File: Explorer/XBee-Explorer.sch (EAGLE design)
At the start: 31 parts, among them U2 XBEE-1B3, U3 MIC5205 3.3V, U4 FT231XS, X1 USBSMD

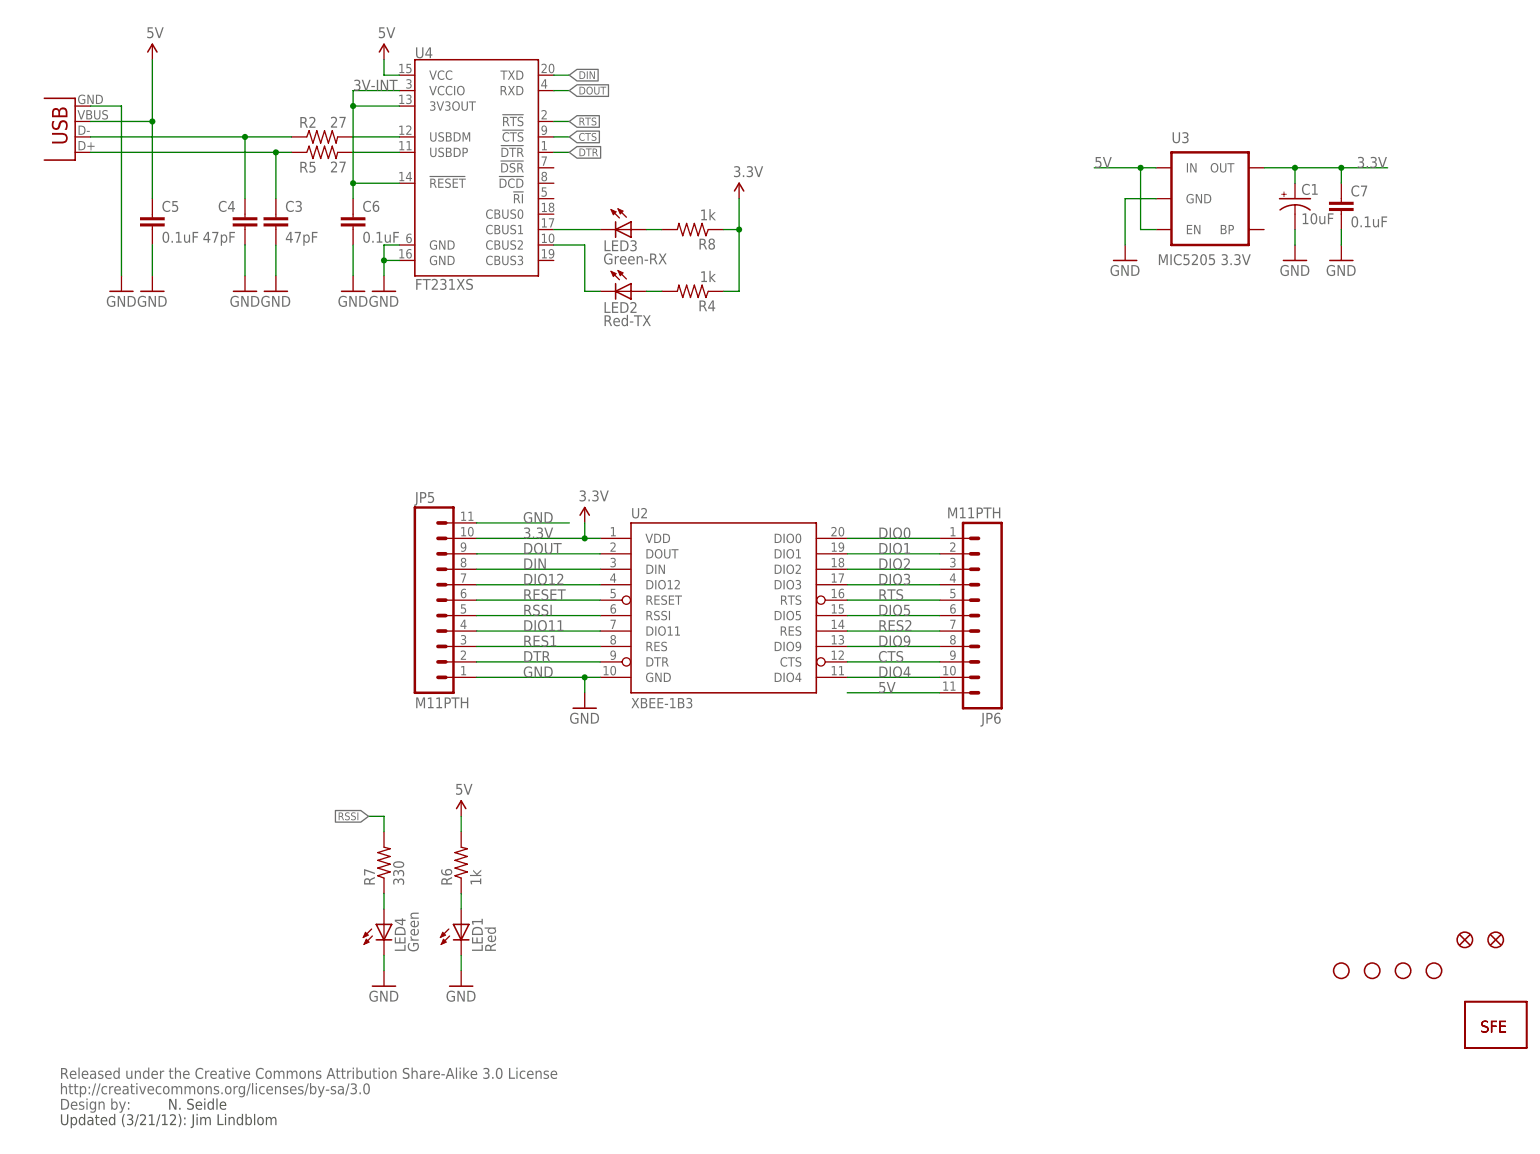
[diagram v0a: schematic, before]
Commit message: Added jumper to disconnect RSSI LED, moved silk
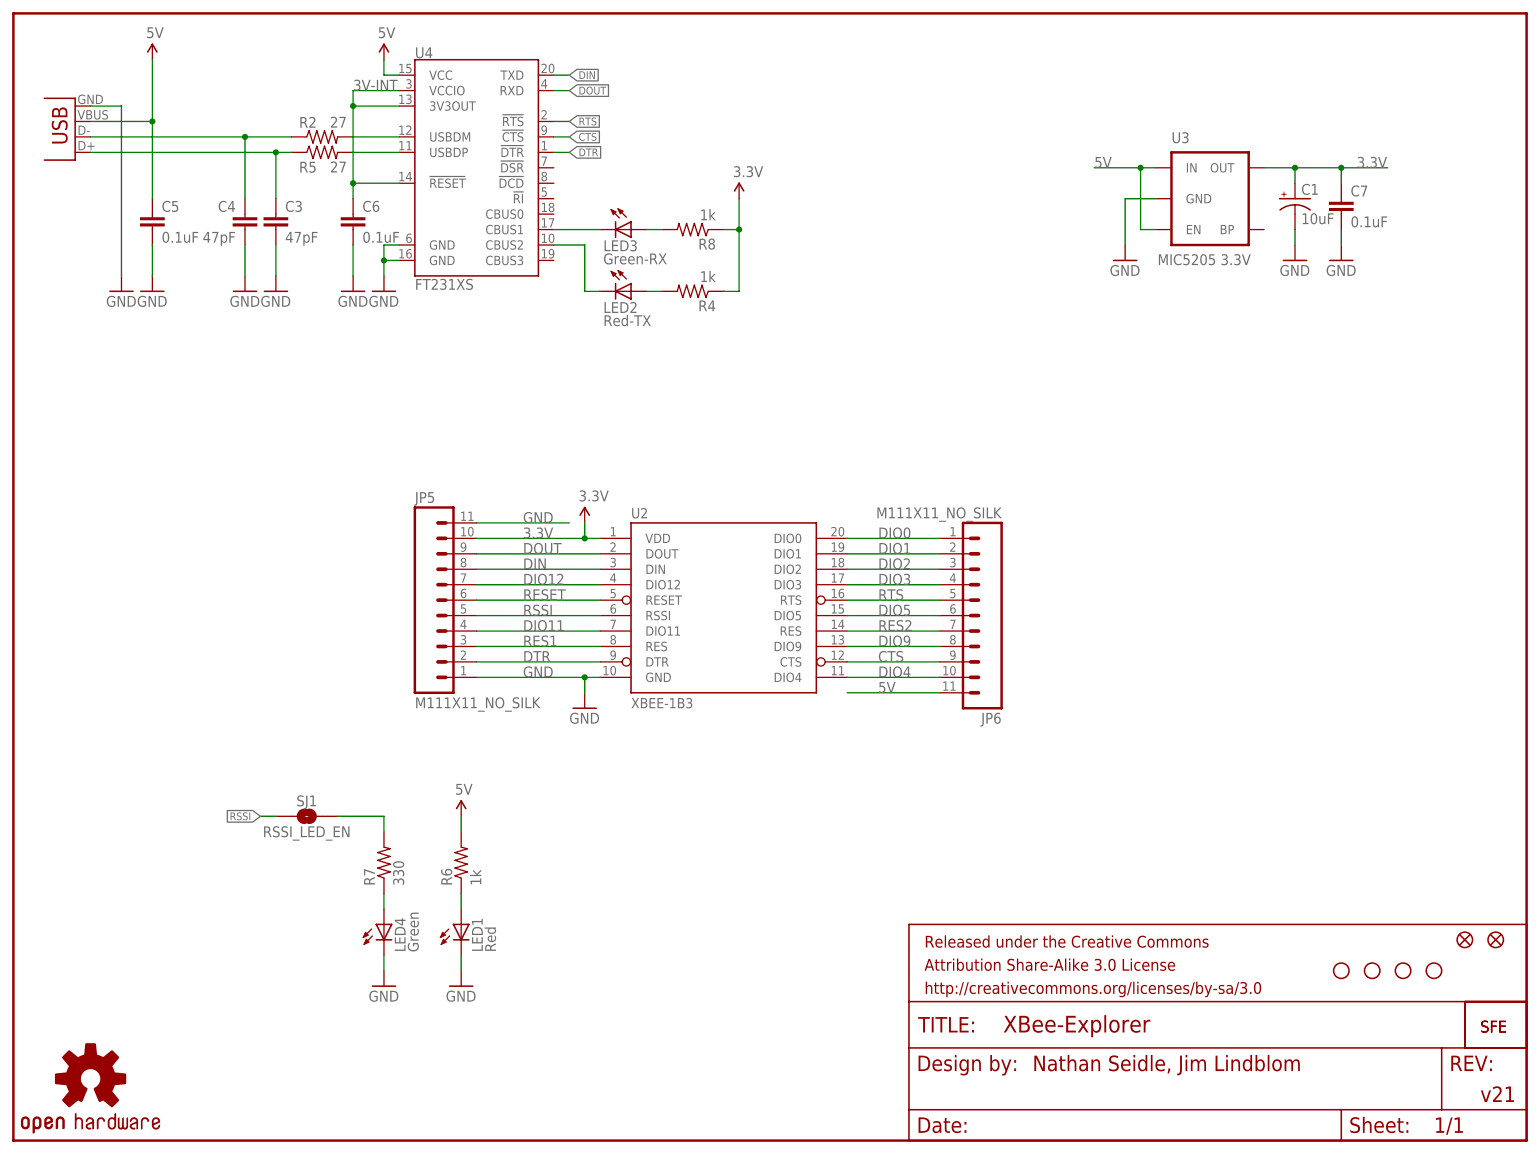
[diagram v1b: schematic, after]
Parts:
- removed U$2: CREATIVE_COMMONS, SparkFun:CREATIVE_COMMONS
- added FRAME1: FRAME-LETTER, SparkFun-Aesthetics:FRAME-LETTER
- added LOGO1: OSHW-LOGOS, SparkFun-Aesthetics:OSHW-LOGOS
- added SJ1: RSSI_LED_EN, SparkFun-Passives:SOLDERJUMPERTRACE
- JP5, JP6: value M11PTH -> M111X11_NO_SILK; device SparkFun-Connectors:M11PTH -> SparkFun-Connectors:M111X11_NO_SILK
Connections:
- new net N$9: R7.2, SJ1.2
- net RSSI: now also SJ1.1; no longer R7.2
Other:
- note added: "Nathan Seidle, Jim Lindblom"
- note added: "v21"
- note removed: "N. Seidle"
- note removed: "Updated (3/21/12): Jim Lindblom"

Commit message: Adding reset button, jumpers on UART ctrl lines
Reset button required moving LEDs around.
Adding jumpers on DTR, CTS, and RTS because they're not present on some
XBee compatible boards. Those pins can be used as GPIOs.
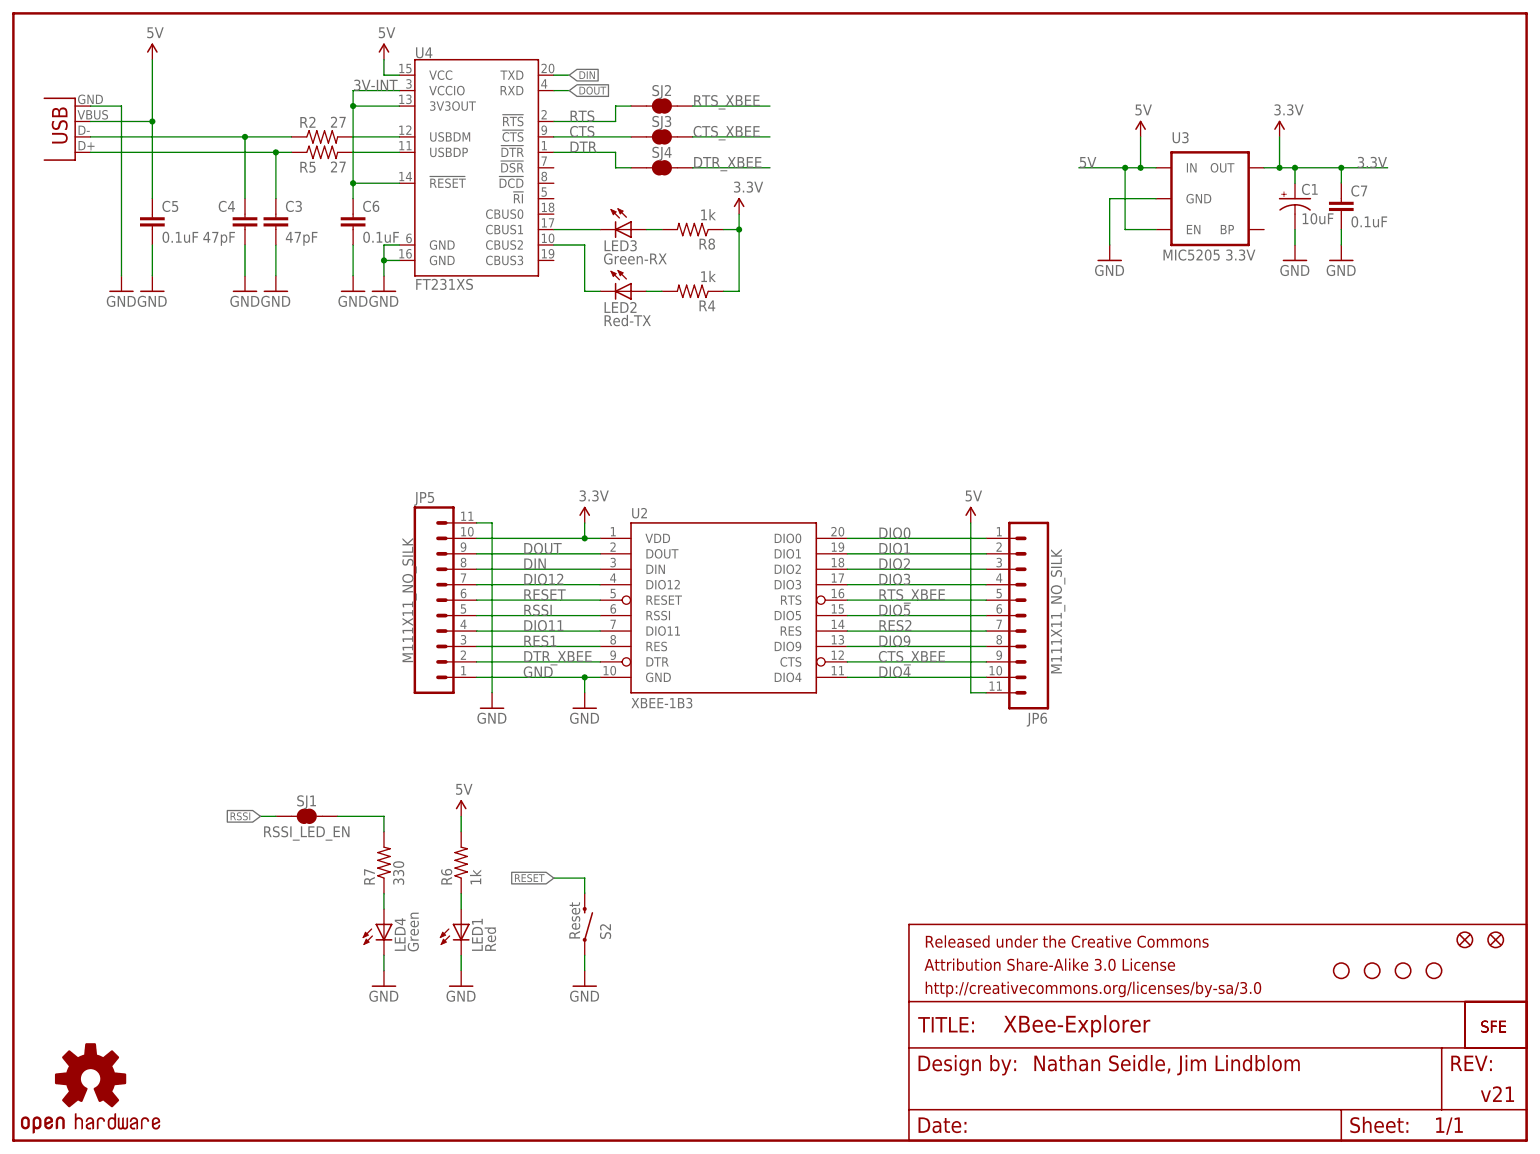
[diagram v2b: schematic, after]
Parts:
- added S2: Reset, SparkFun-Electromechanical:SWITCH-MOMENTARY-2SMD
- added SJ2: CTS_EN, SparkFun-Passives:SOLDERJUMPERTRACE
- added SJ3: RTS_EN, SparkFun-Passives:SOLDERJUMPERTRACE
- added SJ4: DTR, SparkFun-Passives:SOLDERJUMPERTRACE
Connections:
- new net CTS_XBEE: JP6.9, SJ3.2, U2.CTS
- new net DTR_XBEE: JP5.2, SJ4.2, U2.DTR
- new net RTS_XBEE: JP6.5, SJ2.2, U2.RTS
- net CTS: now also SJ3.1; no longer JP6.9, U2.CTS
- net DTR: now also SJ4.1; no longer JP5.2, U2.DTR
- net GND: now also S2.1
- net RESET: now also S2.2
- net RTS: now also SJ2.1; no longer JP6.5, U2.RTS
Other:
- moved on the sheet: JP6

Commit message: Increasing fiducial size and LED footprint
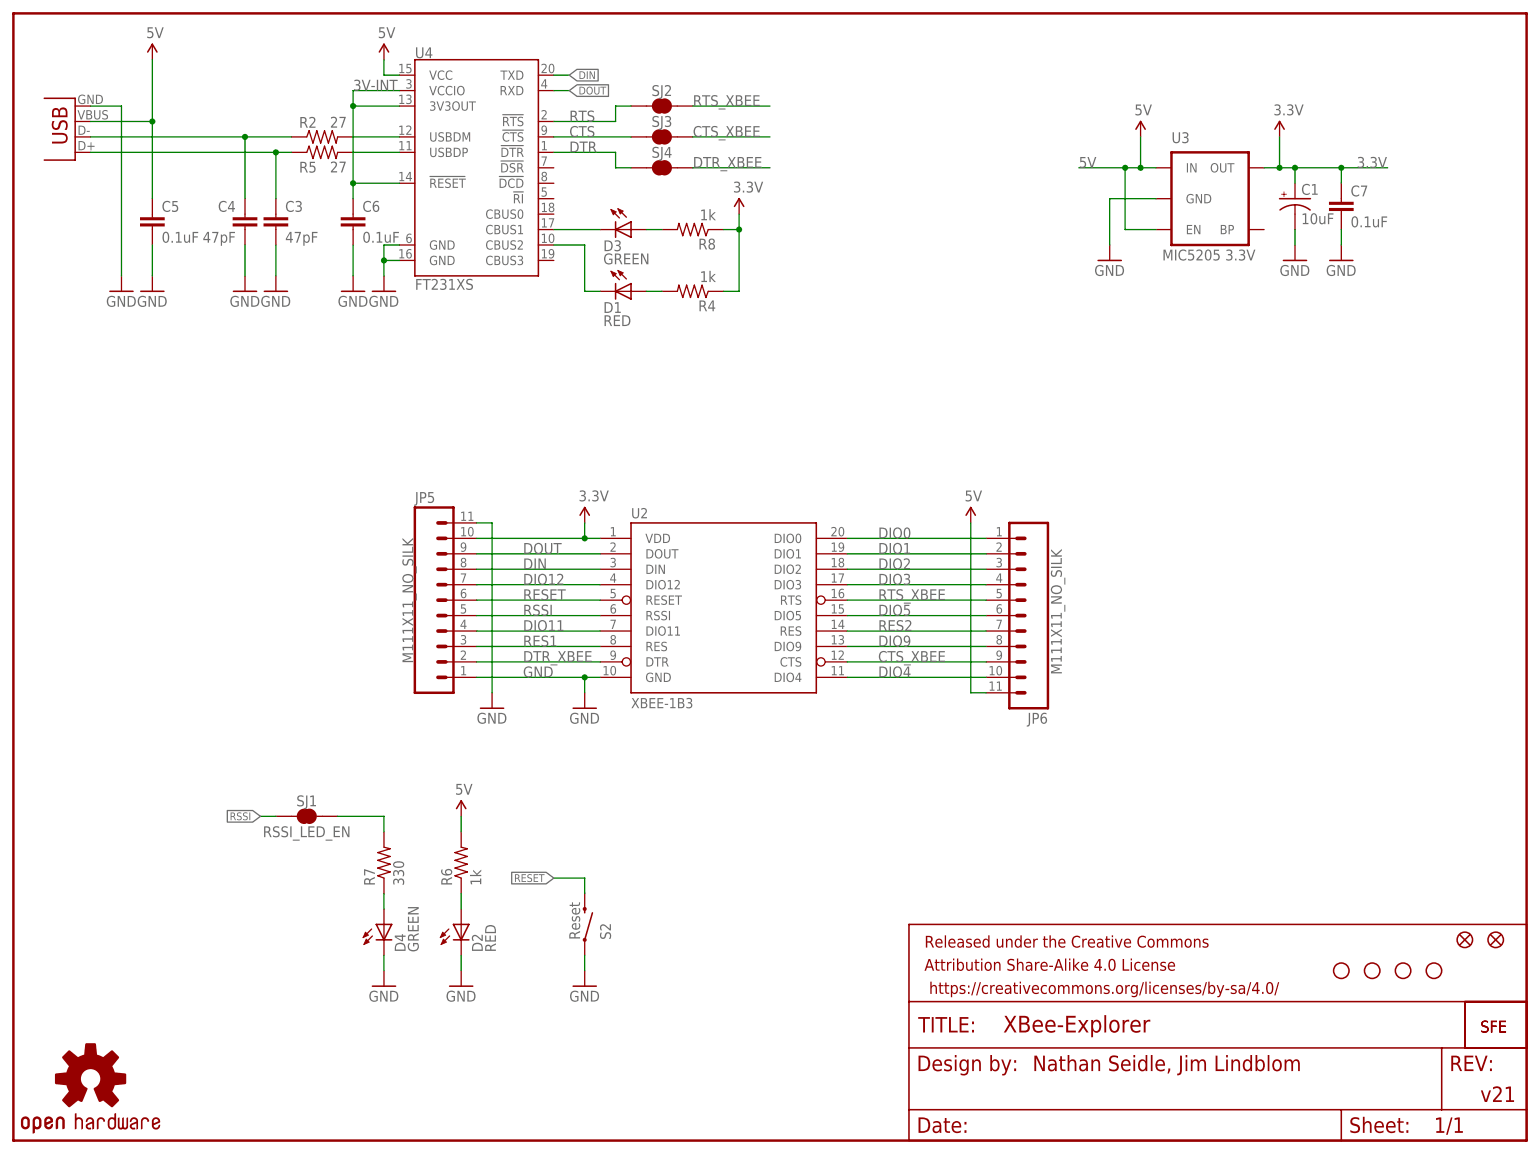
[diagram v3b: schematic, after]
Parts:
- removed LED1: Red, SparkFun:LED0603
- removed LED2: Red-TX, SparkFun:LED0603
- removed LED3: Green-RX, SparkFun:LED0603
- removed LED4: Green, SparkFun:LED0603
- added D1, D2: RED, SparkFun-LED:LED-RED0603
- added D3, D4: GREEN, SparkFun-LED:LED-GREEN0603
- JP1, JP4: value FIDUCIALUFIDUCIAL -> FIDUCIAL1X2; device SparkFun:FIDUCIALUFIDUCIAL -> SparkFun:FIDUCIAL1X2
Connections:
- net GND: now also D2.C, D4.C; no longer LED1.C, LED4.C
- net N$1: now also D1.A; no longer LED2.A
- net N$2: now also D4.A; no longer LED4.A
- net N$38: now also D2.A; no longer LED1.A
- net N$4: now also D3.A; no longer LED3.A
- net N$6: now also D3.C; no longer LED3.C
- net TXLED: now also D1.C; no longer LED2.C
